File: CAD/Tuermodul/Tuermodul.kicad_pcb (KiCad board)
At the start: 2 copper layers, 202.2 x 100 mm, 125 parts, among them J101 Conn_02x16_Counter_Clockwise, J201 Conn_02x25_Counter_Clockwise, J301 Conn_02x25_Counter_Clockwise, Q205 Q_NPN_CBE, Q206 Q_NPN_CBE, Q207 Q_NPN_CBE, Q208 Q_NPN_CBE, Q209 Q_PMOS_GDS, Q210 Q_PMOS_GDS, Q211 Q_PMOS_GDS, Q212 Q_PMOS_GDS, Q213 Q_NPN_CBE, Q214 Q_NPN_CBE, Q215 Q_NPN_CBE, Q216 Q_NPN_CBE, Q301 Q_NPN_CBE, SW301 SW_SPDT_MSM, SW302 SW_SPDT_MSM, SW303 SW_SPDT_MSM, SW304 SW_SPDT_MSM, U101 93LC46B, U102 74HC595, U103 FT4232H, U104 MCP1825S, Y101 12MHz

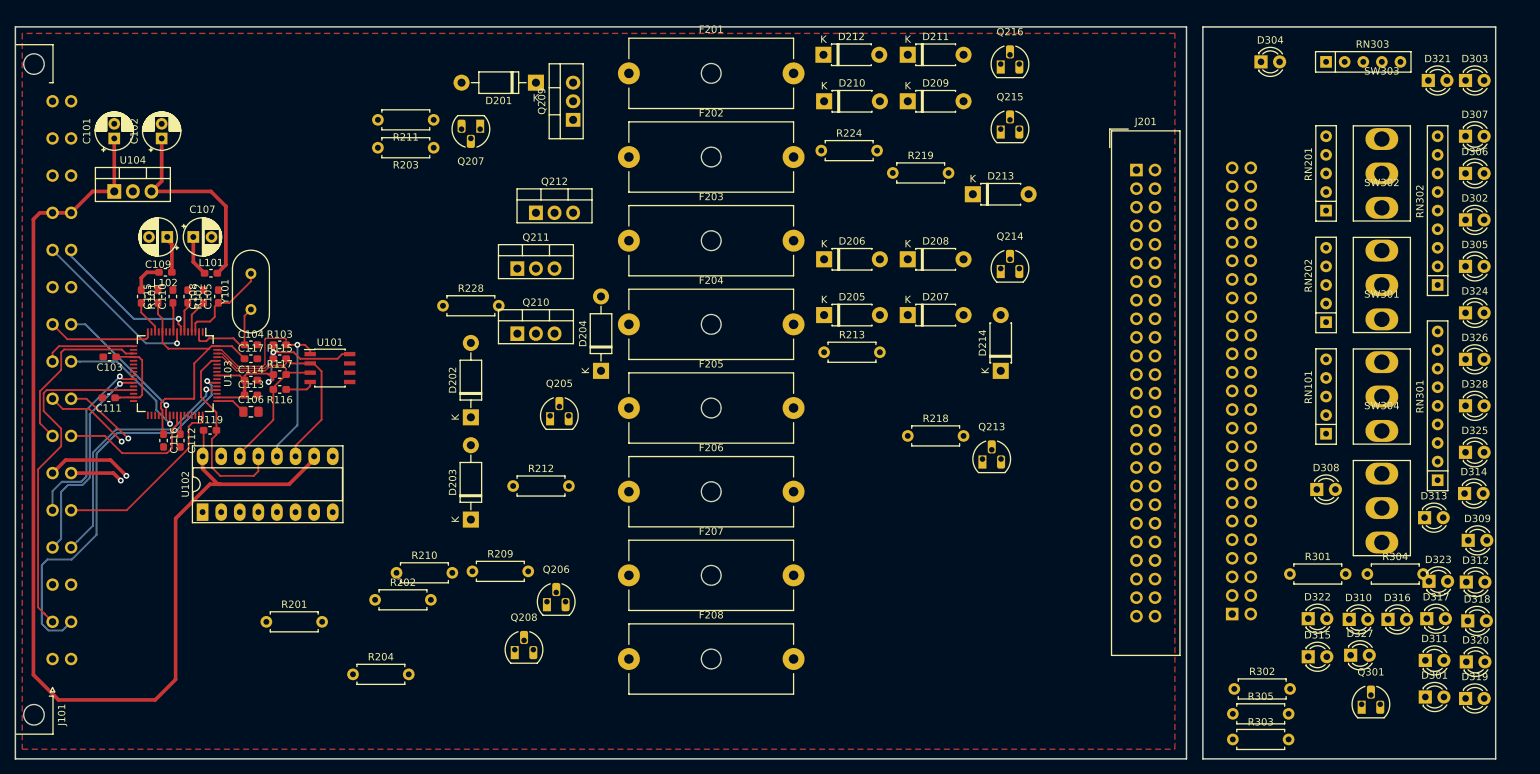
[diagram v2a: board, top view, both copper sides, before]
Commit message: -mod: layout tuermodul
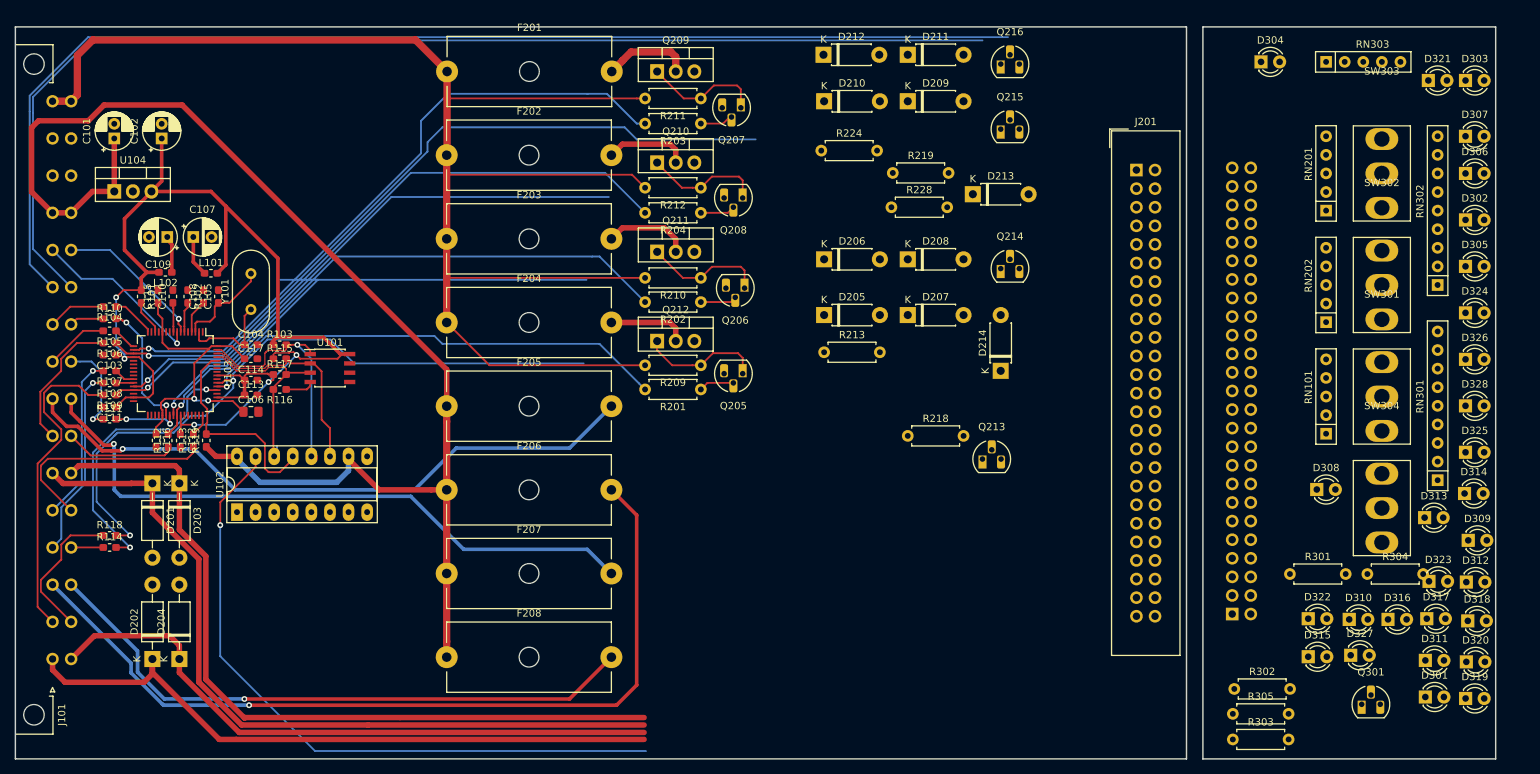
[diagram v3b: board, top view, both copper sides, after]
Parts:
- added R104: 33R, Resistor_SMD:R_0603_1608Metric_Pad1.05x0.95mm_HandSolder, F.Cu at (77.6, 82.7)
- added R105: 33R, Resistor_SMD:R_0603_1608Metric_Pad1.05x0.95mm_HandSolder, F.Cu at (77.6, 86.0)
- added R106: 33R, Resistor_SMD:R_0603_1608Metric_Pad1.05x0.95mm_HandSolder, F.Cu at (77.6, 87.6)
- added R107: 33R, Resistor_SMD:R_0603_1608Metric_Pad1.05x0.95mm_HandSolder, F.Cu at (77.6, 91.4)
- added R108: 33R, Resistor_SMD:R_0603_1608Metric_Pad1.05x0.95mm_HandSolder, F.Cu at (77.6, 93.1)
- added R109: 33R, Resistor_SMD:R_0603_1608Metric_Pad1.05x0.95mm_HandSolder, F.Cu at (77.6, 94.7)
- added R110: 33R, Resistor_SMD:R_0603_1608Metric_Pad1.05x0.95mm_HandSolder, F.Cu at (77.6, 84.3)
- added R111: 33R, Resistor_SMD:R_0603_1608Metric_Pad1.05x0.95mm_HandSolder, F.Cu at (77.6, 98.0)
- added R112: 33R, Resistor_SMD:R_0603_1608Metric_Pad1.05x0.95mm_HandSolder, F.Cu at (85.6, 101.0)
- added R113: 33R, Resistor_SMD:R_0603_1608Metric_Pad1.05x0.95mm_HandSolder, F.Cu at (89.1, 101.0)
- added R114: 33R, Resistor_SMD:R_0603_1608Metric_Pad1.05x0.95mm_HandSolder, F.Cu at (77.6, 115.6)
- added R118: 33R, Resistor_SMD:R_0603_1608Metric_Pad1.05x0.95mm_HandSolder, F.Cu at (77.6, 113.9)
- moved R204 79.0 mm to (158.4, 69.9), turned to 180 degrees
- moved D201 75.8 mm to (83.5, 106.8), turned to 270 degrees
- moved D204 69.8 mm to (87.2, 130.8)
- moved Q208 69.1 mm to (164.1, 67.8), turned to 180 degrees
- moved R201 67.3 mm to (158.4, 94.0), turned to 180 degrees
- moved R228 62.7 mm to (184.5, 69.1)
- moved R202 60.3 mm to (158.4, 82.0), turned to 180 degrees
- moved R210 57.9 mm to (158.4, 78.7), turned to 180 degrees
- moved D202 54.6 mm to (83.5, 130.8)
- moved Q206 50.6 mm to (164.4, 80.1), turned to 180 degrees
- moved R212 48.2 mm to (158.4, 66.4), turned to 180 degrees
- moved R209 42.0 mm to (158.4, 90.7), turned to 180 degrees
- moved D203 40.1 mm to (87.2, 106.8), turned to 270 degrees
- moved R203 36.6 mm to (158.4, 57.7)
- moved R211 36.6 mm to (158.4, 54.2)
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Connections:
- J101 pad 10: /DoorA_MK -> Net-(J101-Pad10)
- J101 pad 12: /DoorB_TX_DTE -> Net-(J101-Pad12)
- J101 pad 13: /DoorB_RX_DTE -> Net-(J101-Pad13)
- J101 pad 15: /DoorB_MK -> Net-(J101-Pad15)
- J101 pad 18: /DoorD_MK -> Net-(J101-Pad18)
- J101 pad 20: /DoorD_RX_DTE -> Net-(J101-Pad20)
- J101 pad 21: /DoorD_TX_DTE -> Net-(J101-Pad21)
- J101 pad 23: /DoorC_MK -> Net-(J101-Pad23)
- J101 pad 25: /DoorC_RX_DTE -> Net-(J101-Pad25)
- J101 pad 26: /DoorC_TX_DTE -> Net-(J101-Pad26)
- J101 pad 7: /DoorA_TX_DTE -> Net-(J101-Pad7)
- J101 pad 8: /DoorA_RX_DTE -> Net-(J101-Pad8)
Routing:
- net +12V: track 0.00 -> 208.3 mm
- net /Error: track 0.00 -> 164.4 mm
- net /UID: track 0.00 -> 161.1 mm
- net /DoorB_VCC: track 0.00 -> 116.6 mm, vias 0 -> 1
- net /DoorC_Lock: track 7.20 -> 107.7 mm, vias 1 -> 0
- net /DoorA_Lock: track 11.7 -> 107.3 mm, vias 1 -> 0
- net /DA_Tx: track 0.00 -> 92.8 mm, vias 0 -> 1
- net /DoorB_Lock: track 0.00 -> 91.1 mm
- net /DoorA_RTS: track 0.00 -> 89.0 mm, vias 0 -> 1
- net /DoorD_Lock: track 0.00 -> 87.2 mm
- net /DoorD_VCC: track 0.00 -> 84.3 mm, vias 0 -> 1
- net /DoorB_RTS: track 0.00 -> 84.2 mm, vias 0 -> 1
- net /DoorA_MK: track 23.6 -> 102.5 mm, vias 0 -> 1
- net /DoorC_VCC: track 10.3 -> 88.6 mm
- net /DoorC_RTS: track 0.00 -> 77.1 mm, vias 0 -> 1
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- removed copper zone on F.Cu, net GND

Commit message: -mod: adapted TechSpec due to power enable discussion -mod: changed pin header for front-to-main panel connection -mod: general layout work
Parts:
- removed D302: rt, LED_THT:LED_D3.0mm
- removed R303: 330R, Resistor_THT:R_Axial_DIN0207_L6.3mm_D2.5mm_P7.62mm_Horizontal
- added R205: 10k, Resistor_SMD:R_0603_1608Metric_Pad1.05x0.95mm_HandSolder, F.Cu at (76.5, 72.3)
- J201, J301: value Conn_02x25_Counter_Clockwise -> Conn_02x20_Counter_Clockwise; footprint Connector_IDC:IDC-Header_2x25_P2.54mm_Vertical -> Connector_PinSocket_2.54mm:PinSocket_2x20_P2.54mm_Vertical_SMD
- moved RN202 89.1 mm to (162.5, 121.2)
- moved D212 85.7 mm to (151.3, 130.6)
- moved D211 79.2 mm to (151.3, 119.1)
- moved RN201 70.0 mm to (173.9, 73.7)
- moved RN101 65.8 mm to (191.9, 140.5), turned to 180 degrees
- moved Q216 58.4 mm to (178.4, 104.0), turned to 270 degrees
- moved D210 58.0 mm to (151.2, 107.4)
- moved D209 55.6 mm to (151.1, 97.3)
- moved J201 52.8 mm to (203.2, 114.7)
- moved D213 47.9 mm to (169.3, 107.4), turned to 180 degrees
- moved R224 46.3 mm to (174.2, 107.7), turned to 270 degrees
- moved Q215 46.3 mm to (179.4, 100.2), turned to 90 degrees
- moved Q214 46.3 mm to (170.1, 113.3), turned to 180 degrees
- moved R219 40.0 mm to (161.8, 97.3)
- moved J301 39.3 mm to (238.6, 86.1)
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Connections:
- J101 pad 27: /UID -> /~PWR_EN~
- J201 pad 10: /DoorA_MK -> /Peripherie/DoorA_12V
- J201 pad 11: /Peripherie/DoorA_12V -> /DoorA_VCC
- J201 pad 12: /DoorA_VCC -> /DC_Tx
- J201 pad 13: /DC_Tx -> /DC_Rx
- J201 pad 14: /DC_Rx -> /DoorC_Lock
- J201 pad 15: /DoorC_Lock -> /Peripherie/DoorC_Auto
- J201 pad 16: /Peripherie/DoorC_Auto -> /DoorC_MK
- J201 pad 17: /DoorC_MK -> /Peripherie/DoorC_12V
- J201 pad 18: /Peripherie/DoorC_12V -> /DoorC_VCC
- J201 pad 19: /DoorC_VCC -> (no net)
- J201 pad 23: (no net) -> /DoorD_VCC
- J201 pad 24: (no net) -> /Peripherie/DoorD_12V
- J201 pad 25: (no net) -> /DoorD_MK
- J201 pad 26: (no net) -> /Peripherie/DoorD_Auto
- J201 pad 27: (no net) -> /DoorD_Lock
- J201 pad 28: (no net) -> /DD_Rx
- J201 pad 29: (no net) -> /DD_Tx
- J201 pad 30: (no net) -> /DoorB_VCC
- J201 pad 31: (no net) -> /Peripherie/DoorB_12V
- J201 pad 32: /DoorD_VCC -> /DoorB_MK
- J201 pad 33: /Peripherie/DoorD_12V -> /Peripherie/DoorB_Auto
- J201 pad 34: /DoorD_MK -> /DoorB_Lock
- J201 pad 35: /Peripherie/DoorD_Auto -> /DB_Rx
- J201 pad 36: /DoorD_Lock -> /DB_Tx
- J201 pad 37: /DD_Rx -> (no net)
- J201 pad 38: /DD_Tx -> (no net)
- J201 pad 39: /DoorB_VCC -> (no net)
- J201 pad 40: /Peripherie/DoorB_12V -> (no net)
- J201 pad 5: /UID -> /DA_Tx
- J201 pad 6: /DA_Tx -> /DA_Rx
- J201 pad 7: /DA_Rx -> /DoorA_Lock
- J201 pad 8: /DoorA_Lock -> /Peripherie/DoorA_Auto
- J201 pad 9: /Peripherie/DoorA_Auto -> /DoorA_MK
- J301 pad 10: /Front/DoorA_MK -> /Front/DoorA_12V
- J301 pad 11: /Front/DoorA_12V -> /Front/DoorA_VCC
- J301 pad 12: /Front/DoorA_VCC -> /Front/DC_Tx
- J301 pad 13: /Front/DC_Tx -> /Front/DC_Rx
- J301 pad 14: /Front/DC_Rx -> /Front/DoorC_Lock
- J301 pad 15: /Front/DoorC_Lock -> /Front/DoorC_Auto
- J301 pad 16: /Front/DoorC_Auto -> /Front/DoorC_MK
- J301 pad 17: /Front/DoorC_MK -> /Front/DoorC_12V
- J301 pad 18: /Front/DoorC_12V -> /Front/DoorC_VCC
- J301 pad 19: /Front/DoorC_VCC -> (no net)
- J301 pad 23: (no net) -> /Front/DoorD_VCC
- J301 pad 24: (no net) -> /Front/DoorD_12V
- J301 pad 25: (no net) -> /Front/DoorD_MK
- J301 pad 26: (no net) -> /Front/DoorD_Auto
- J301 pad 27: (no net) -> /Front/DoorD_Lock
- J301 pad 28: (no net) -> /Front/DD_Rx
- J301 pad 29: (no net) -> /Front/DD_Tx
- J301 pad 30: (no net) -> /Front/DoorB_VCC
- J301 pad 31: (no net) -> /Front/DoorB_12V
- J301 pad 32: /Front/DoorD_VCC -> /Front/DoorB_MK
- J301 pad 33: /Front/DoorD_12V -> /Front/DoorB_Auto
- J301 pad 34: /Front/DoorD_MK -> /Front/DoorB_Lock
- J301 pad 35: /Front/DoorD_Auto -> /Front/DB_Rx
- J301 pad 36: /Front/DoorD_Lock -> /Front/DB_Tx
- J301 pad 37: /Front/DD_Rx -> (no net)
- J301 pad 38: /Front/DD_Tx -> (no net)
- J301 pad 39: /Front/DoorB_VCC -> (no net)
- J301 pad 40: /Front/DoorB_12V -> (no net)
- J301 pad 5: /Front/UID -> /Front/DA_Tx
- J301 pad 6: /Front/DA_Tx -> /Front/DA_Rx
- J301 pad 7: /Front/DA_Rx -> /Front/DoorA_Lock
- J301 pad 8: /Front/DoorA_Lock -> /Front/DoorA_Auto
- J301 pad 9: /Front/DoorA_Auto -> /Front/DoorA_MK
- Q205 pad 3: GND -> /~PWR_EN~
- Q206 pad 3: GND -> /~PWR_EN~
- Q207 pad 3: GND -> /~PWR_EN~
- Q208 pad 3: GND -> /~PWR_EN~
- Q209 pad 2: /Peripherie/DoorA_12V -> /Peripherie/DoorA_Auto
- Q209 pad 3: /Peripherie/DoorA_Auto -> /Peripherie/DoorA_12V
- Q210 pad 2: /Peripherie/DoorB_12V -> /Peripherie/DoorB_Auto
- Q210 pad 3: /Peripherie/DoorB_Auto -> /Peripherie/DoorB_12V
- Q211 pad 2: /Peripherie/DoorC_12V -> /Peripherie/DoorC_Auto
- Q211 pad 3: /Peripherie/DoorC_Auto -> /Peripherie/DoorC_12V
- Q212 pad 2: /Peripherie/DoorD_12V -> /Peripherie/DoorD_Auto
- Q212 pad 3: /Peripherie/DoorD_Auto -> /Peripherie/DoorD_12V
- R301 pad 1: +5V -> +5P
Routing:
- net /~PWR_EN~: track 0.00 -> 213.6 mm, vias 0 -> 1
- net /UID: track 161.1 -> 0.00 mm
- net +5V: track 182.2 -> 259.7 mm
- net +12V: track 208.3 -> 262.3 mm
- net Net-(D205-Pad2): track 0.00 -> 47.5 mm
- net Net-(D209-Pad2): track 0.00 -> 39.5 mm
- net /Peripherie/DoorD_12V: track 10.9 -> 43.1 mm
- net /DoorD_VCC: track 84.3 -> 112.4 mm
- net /DoorB_VCC: track 116.6 -> 144.1 mm
- net /DoorA_VCC: track 87.5 -> 112.7 mm
- net /Peripherie/DoorA_12V: track 12.1 -> 37.1 mm
- net /Peripherie/DoorC_12V: track 11.8 -> 33.8 mm
- net /Error: track 164.4 -> 185.9 mm
- net /Peripherie/DoorB_12V: track 11.5 -> 31.9 mm
- net /DoorC_VCC: track 88.6 -> 106.9 mm
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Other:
- board size 202.2 x 100 mm -> 202.2 x 100.1 mm

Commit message: mod:layout work
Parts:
- moved F208 82.3 mm to (115.1, 48.7), turned to 270 degrees
- moved F201 71.4 mm to (195.1, 48.8), turned to 270 degrees
- moved F207 70.5 mm to (126.5, 48.7), turned to 270 degrees
- moved D322 68.9 mm to (240.3, 56.4)
- moved RN101 65.8 mm to (133.9, 109.5), turned to 0 degrees
- moved D212 65.2 mm to (115.1, 76.3), turned to 270 degrees
- moved F202 61.4 mm to (183.7, 48.7), turned to 270 degrees
- moved F206 60.7 mm to (138.0, 48.7), turned to 270 degrees
- moved F203 54.5 mm to (172.3, 48.7), turned to 270 degrees
- moved F205 54.1 mm to (149.4, 48.7), turned to 270 degrees
- moved F204 51.8 mm to (160.8, 48.7), turned to 270 degrees
- moved RN202 50.7 mm to (124.5, 87.5), turned to 0 degrees
- moved Q209 50.5 mm to (195.1, 77.5), turned to 270 degrees
- moved D211 49.4 mm to (126.5, 76.3), turned to 270 degrees
- moved D205 49.3 mm to (195.2, 87.0), turned to 270 degrees
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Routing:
- net +5V: track 259.7 -> 417.7 mm, vias 0 -> 2
- net /DA_Rx: track 0.00 -> 115.4 mm, vias 0 -> 1
- net +12V: track 262.3 -> 371.4 mm
- net /DC_Tx: track 0.00 -> 100.2 mm, vias 0 -> 1
- net /DoorD_VCC: track 112.4 -> 209.8 mm, vias 1 -> 5
- net /DoorC_VCC: track 106.9 -> 202.4 mm, vias 1 -> 4
- net /DC_Rx: track 0.00 -> 92.6 mm, vias 0 -> 1
- net /DoorA_MK: track 86.2 -> 168.6 mm, vias 1 -> 4
- net /DoorD_MK: track 93.4 -> 169.4 mm, vias 2 -> 5
- net /DD_Rx: track 0.00 -> 72.5 mm, vias 0 -> 2
- net /DD_Tx: track 0.00 -> 70.9 mm, vias 0 -> 1
- net /DoorA_VCC: track 112.7 -> 182.6 mm, vias 1 -> 4
- net /DB_Tx: track 0.00 -> 68.6 mm
- net /Peripherie/DoorB_Auto: track 0.00 -> 65.1 mm, vias 0 -> 2
- net /DB_Rx: track 0.00 -> 64.5 mm, vias 0 -> 1
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- added copper zone on B.Cu, net GND
- added copper zone on F.Cu, net GND
